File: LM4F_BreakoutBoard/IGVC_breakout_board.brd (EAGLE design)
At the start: 79.7 x 80 mm, 20 parts, among them IC1 7407N

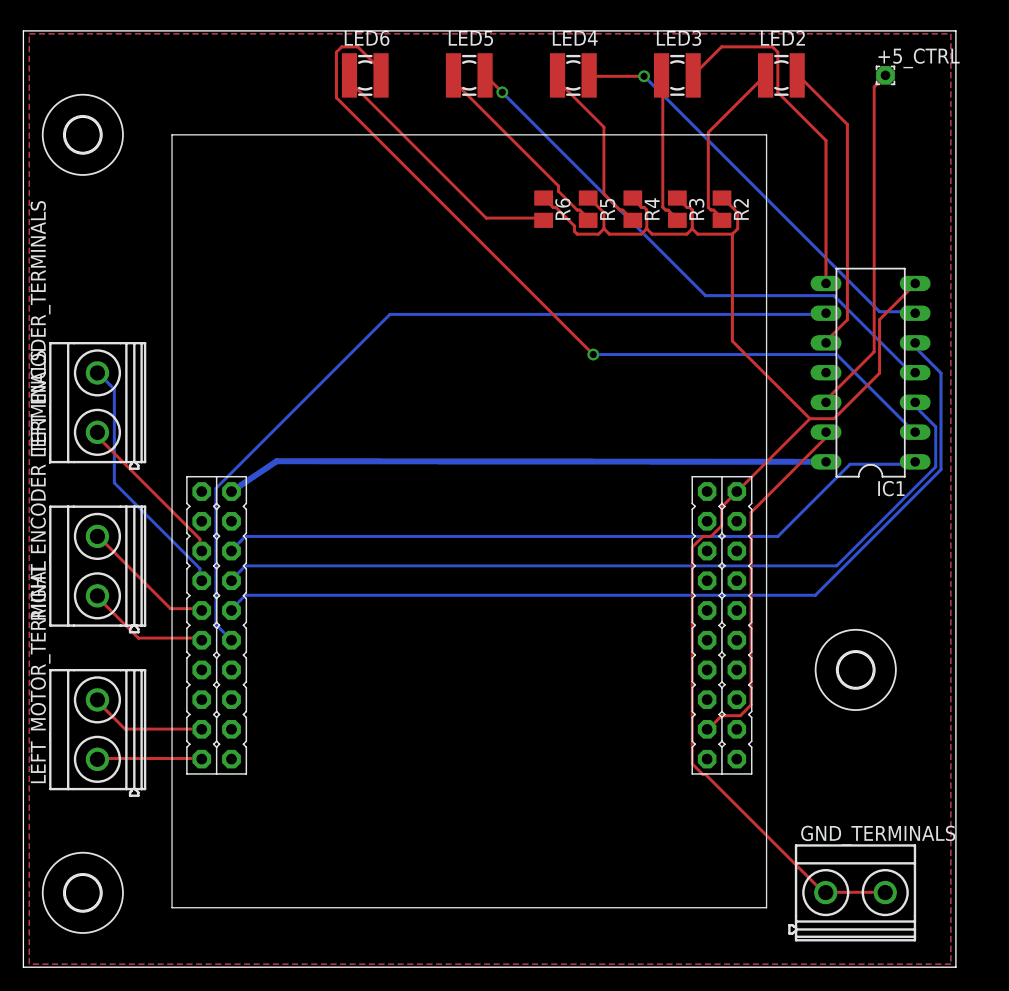
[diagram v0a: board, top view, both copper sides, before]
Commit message: re-routed board to be much smaller
* we now have a ground plane!
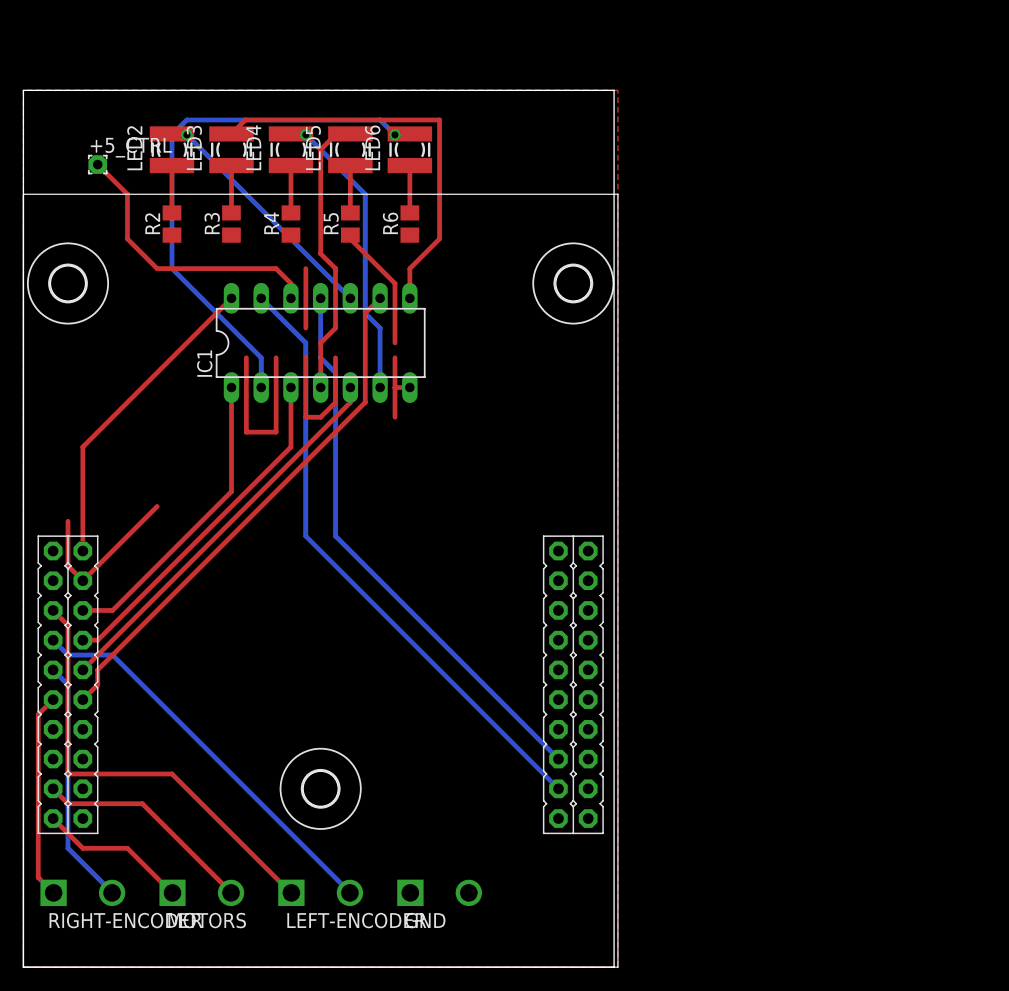
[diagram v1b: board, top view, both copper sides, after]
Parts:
- removed GND_TERMINALS, LEFT_ENCODER_TERMINALS, LEFT_MOTOR_TERMINAL, RIGHT_ENCODER_TERMINALS: MKDSN1,5/2-5,08, con-phoenix-508:MKDSN1,5/2-5,08
- added GND, LEFT-ENCODER, MOTORS, RIGHT-ENCODER: PHOENIXSCREWTERMINAL_2, RASEagleLib:PHOENIXSCREWTERMINAL_2
- moved +5_CTRL 67.7 mm to (6.35, 68.6)
- moved H4 66.8 mm to (47.0, 58.4)
- moved LED2 52.5 mm to (12.7, 69.8), turned to 90 degrees
- moved IC1 47.1 mm to (25.4, 53.3), turned to 0 degrees
- moved R2 47.0 mm to (12.7, 63.5), turned to 90 degrees
- moved H2 46.8 mm to (25.4, 15.2)
- moved LED3 38.6 mm to (17.8, 69.8), turned to 90 degrees
- moved R3 38.1 mm to (17.8, 63.5), turned to 90 degrees
- moved R4 29.2 mm to (22.9, 63.5), turned to 90 degrees
- moved LED4 25.0 mm to (22.9, 69.8), turned to 90 degrees
- moved R5 20.4 mm to (27.9, 63.5), turned to 90 degrees
- moved LM4F 13.7 mm to (0.00, 66.0)
- moved H5 12.8 mm to (3.81, 58.4)
- moved LED5 12.0 mm to (27.9, 69.8), turned to 90 degrees
- moved R6 11.5 mm to (33.0, 63.5), turned to 90 degrees
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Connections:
- net N$20 renamed LEFT
- net N$7 renamed VBUS
- net GND: now also GND.1, GND.2, LM4F.GND1; no longer GND_TERMINALS.1, GND_TERMINALS.2
- net N$1: now also RIGHT-ENCODER.2; no longer RIGHT_ENCODER_TERMINALS.2
- net N$2: now also LM4F.PA6, MOTORS.2; no longer LEFT_MOTOR_TERMINAL.1, LM4F.PA7
- net N$24: now also IC1.11
- net N$3: now also LM4F.PA7, MOTORS.1; no longer LEFT_MOTOR_TERMINAL.2, LM4F.PA6
- net N$4: now also RIGHT-ENCODER.1; no longer RIGHT_ENCODER_TERMINALS.1
- net N$5: now also LEFT-ENCODER.1; no longer LEFT_ENCODER_TERMINALS.1
- net N$6: now also LEFT-ENCODER.2; no longer LEFT_ENCODER_TERMINALS.2
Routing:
- net GND: track 122.5 -> 64.0 mm
- net N$24: track 0.00 -> 47.8 mm
- net N$22: track 77.4 -> 33.6 mm
- net N$21: track 70.5 -> 29.7 mm
- net LEFT: track 61.7 -> 25.8 mm
- net N$23: track 71.9 -> 44.8 mm
- net VBUS: track 51.7 -> 26.9 mm
- net N$19: track 70.5 -> 46.2 mm
- net N$5: track 14.0 -> 37.8 mm
- net N$18: track 47.3 -> 24.5 mm, vias 1 -> 0
- net N$25: track 30.6 -> 52.4 mm
- net N$13: track 22.0 -> 4.05 mm
- net N$12: track 17.3 -> 4.05 mm
- net N$6: track 21.5 -> 34.3 mm
- net N$11: track 15.2 -> 4.05 mm
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- removed copper zone on layer 16, net GND
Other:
- board size 79.7 x 80 mm -> 50.5 x 74.9 mm
- board text removed: "7407"
- board text removed: "GND"
- board text removed: "IEEE RAS IGVC 2015 LM4F Breakout Board"
- board text removed: "Left Encoder"
- board text removed: "Motor Out"
- board text removed: "PA6 Left Motor"
- board text removed: "PA7 Right Motor"
- board text removed: "PD0"
- board text removed: "PD1"
- board text removed: "PD2"
- board text removed: "PD3"
- board text removed: "PD4"
- board text removed: "PD5"
- board text removed: "Right Encoder"

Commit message: re-boarded to fit within 5cm x 5cm
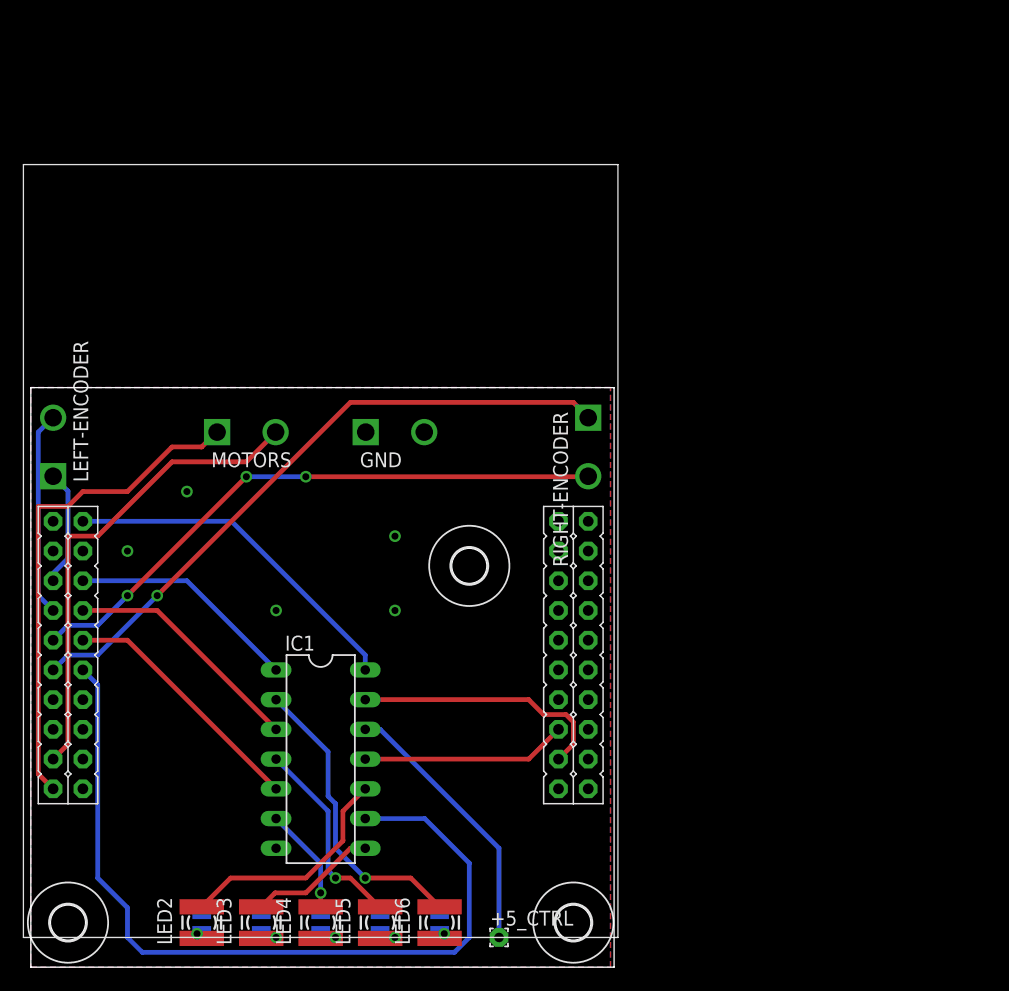
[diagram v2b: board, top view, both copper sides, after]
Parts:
- moved +5_CTRL 74.4 mm to (40.6, 2.54)
- moved LED2 66.1 mm to (15.2, 3.81)
- moved LED3 66.1 mm to (20.3, 3.81)
- moved LED4 66.1 mm to (25.4, 3.81)
- moved LED5 66.1 mm to (30.5, 3.81)
- moved LED6 66.1 mm to (35.6, 3.81)
- moved R2 59.7 mm to (15.2, 3.81), flipped to the bottom, turned to 270 degrees
- moved R3 59.7 mm to (20.3, 3.81), flipped to the bottom, turned to 270 degrees
- moved R4 59.7 mm to (25.4, 3.81), flipped to the bottom, turned to 270 degrees
- moved R5 59.7 mm to (30.5, 3.81), flipped to the bottom, turned to 270 degrees
- moved R6 59.7 mm to (35.6, 3.81), flipped to the bottom, turned to 270 degrees
- moved RIGHT-ENCODER 57.6 mm to (48.3, 44.5), turned to 270 degrees
- moved H5 54.6 mm to (3.81, 3.81)
- moved LEFT-ENCODER 44.4 mm to (2.54, 44.5), turned to 90 degrees
- moved GND 39.6 mm to (31.8, 45.7)
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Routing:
- net GND: track 64.0 -> 0.00 mm, vias 0 -> 5
- net N$4: track 17.6 -> 55.8 mm, vias 0 -> 1
- net N$1: track 21.1 -> 51.5 mm, vias 0 -> 3
- net N$24: track 47.8 -> 17.6 mm
- net N$25: track 52.4 -> 22.3 mm
- net N$3: track 12.8 -> 42.6 mm
- net N$5: track 37.8 -> 9.98 mm
- net N$23: track 44.8 -> 71.5 mm
- net N$16: track 34.6 -> 11.0 mm
- net N$2: track 18.9 -> 41.1 mm
- net N$19: track 46.2 -> 25.8 mm
- net N$6: track 34.3 -> 17.5 mm
- net N$17: track 25.5 -> 9.12 mm
- net N$22: track 33.6 -> 21.8 mm
- net N$21: track 29.7 -> 20.7 mm
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- added copper zone on layer 16, net GND
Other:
- board size 50.5 x 74.9 mm -> 49.8 x 49.5 mm
